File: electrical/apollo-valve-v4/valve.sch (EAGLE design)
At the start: 31 parts, among them J1 VALVE2, J2 VALVE1, U1 DRV8806-SSOP, U2 DRV8806-SSOP, U3 TPS54202

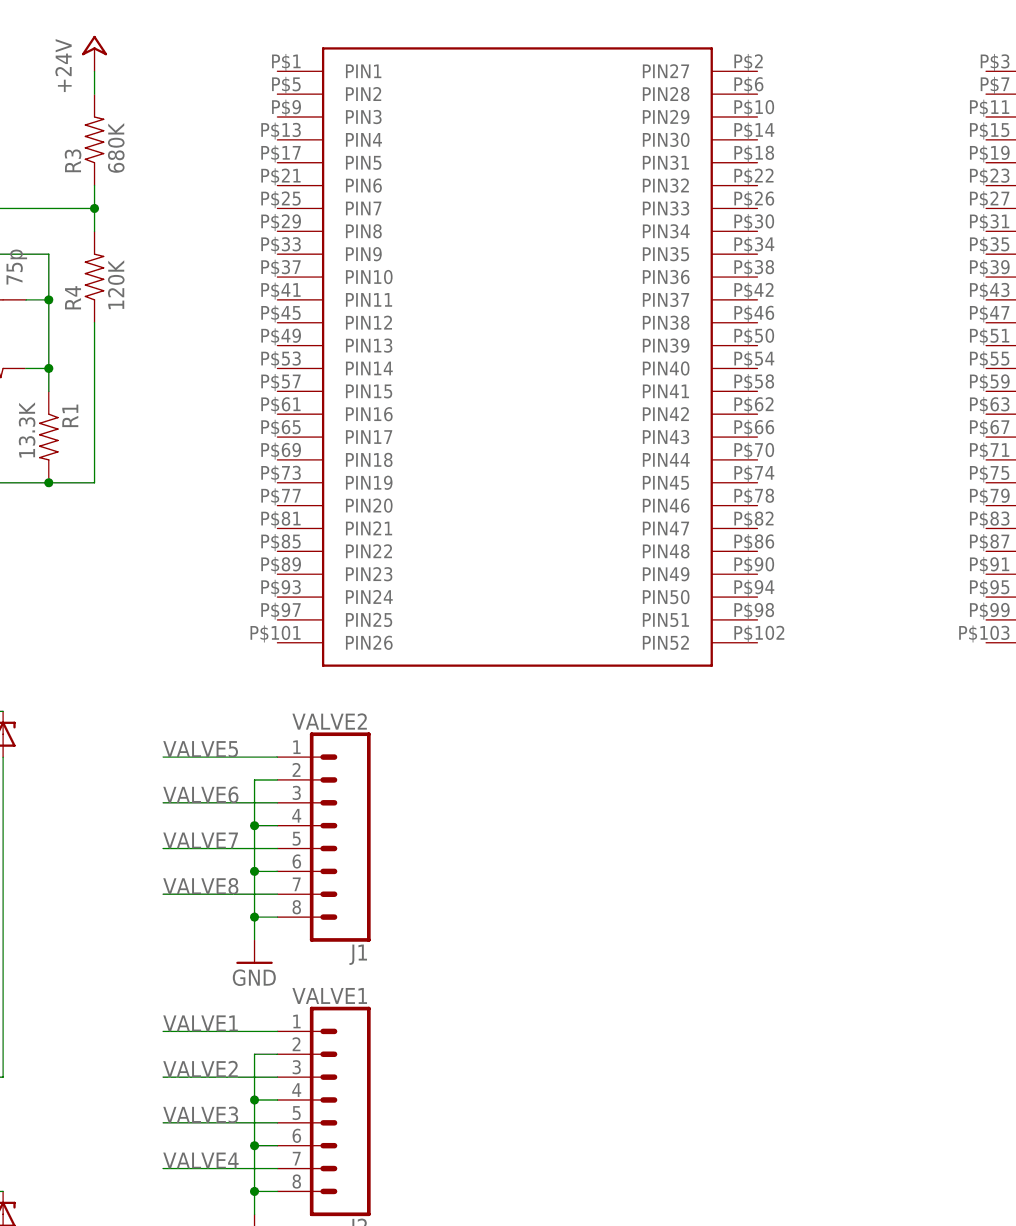
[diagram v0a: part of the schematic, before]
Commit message: Update valve board and proposed a pinout for Apollo v4
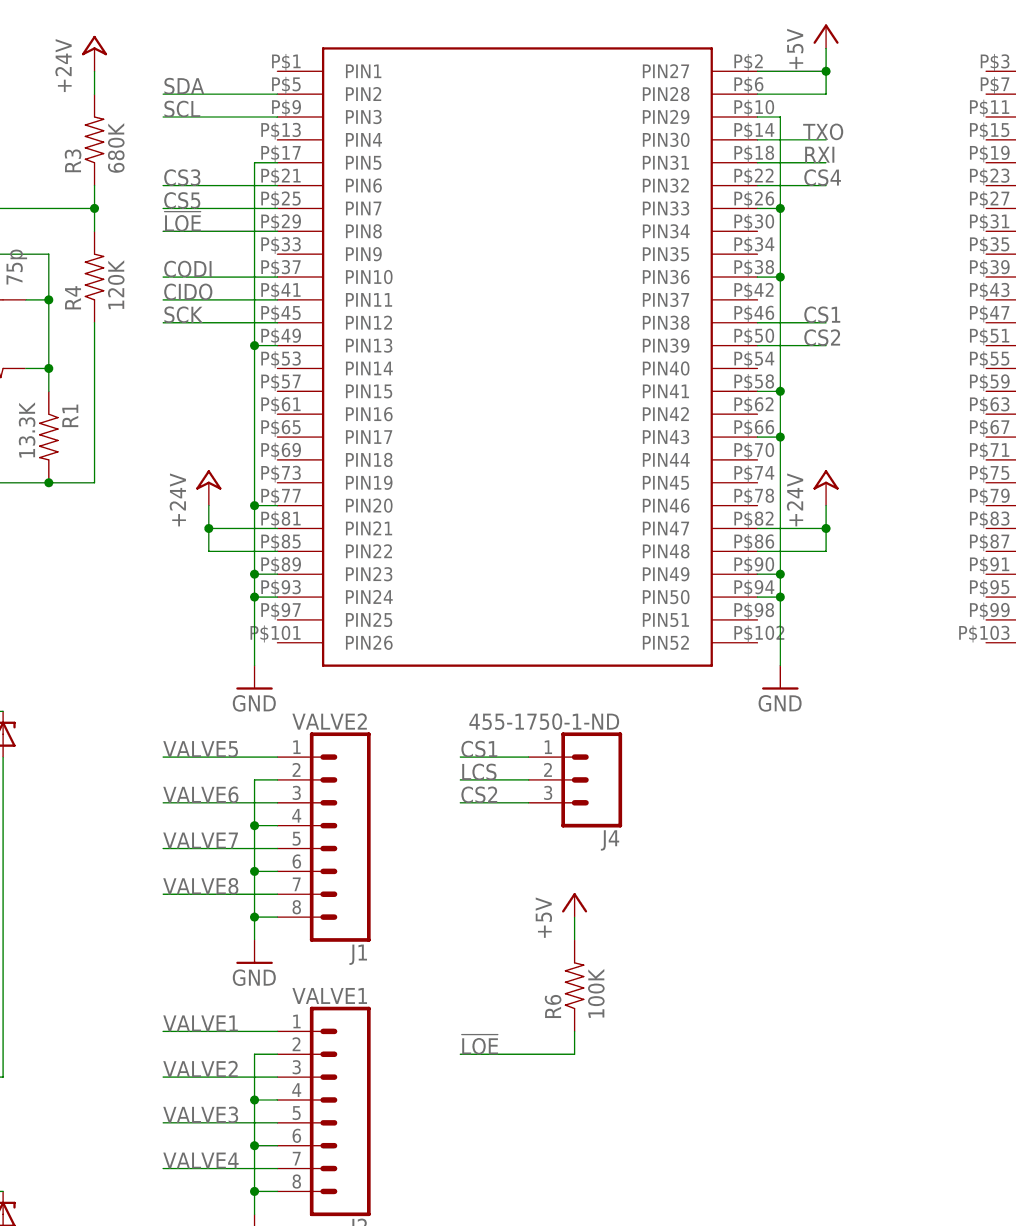
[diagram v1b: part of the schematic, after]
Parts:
- added J4: 455-1750-1-ND, SparkFun-Connectors:CONN_03
- added R6: 100K, apollo-ctrl-v4:RESISTOR0805-RES
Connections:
- new net CIDO: U$1.PIN11
- new net CS1: J4.1, U$1.PIN38
- new net CS2: J4.3, U$1.PIN39
- new net CS3: U$1.PIN6
- new net CS4: U$1.PIN32
- new net CS5: U$1.PIN7
- new net RXI: U$1.PIN31
- new net SCL: U$1.PIN3
- new net SDA: U$1.PIN2
- new net TXO: U$1.PIN30
- net !LOE!: now also R6.1, U$1.PIN8
- net +24V: now also U$1.PIN21, U$1.PIN22, U$1.PIN47, U$1.PIN48
- net +5V: now also R6.2, U$1.PIN27, U$1.PIN28
- net CODI: now also U$1.PIN10
- net GND: now also U$1.PIN13, U$1.PIN20, U$1.PIN23, U$1.PIN24, U$1.PIN29, U$1.PIN33, U$1.PIN36, U$1.PIN41, U$1.PIN43, U$1.PIN49, U$1.PIN5, U$1.PIN50
- net LCS: now also J4.2
- net SCK: now also U$1.PIN12
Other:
- note added: "DEFAULT should be CS1"

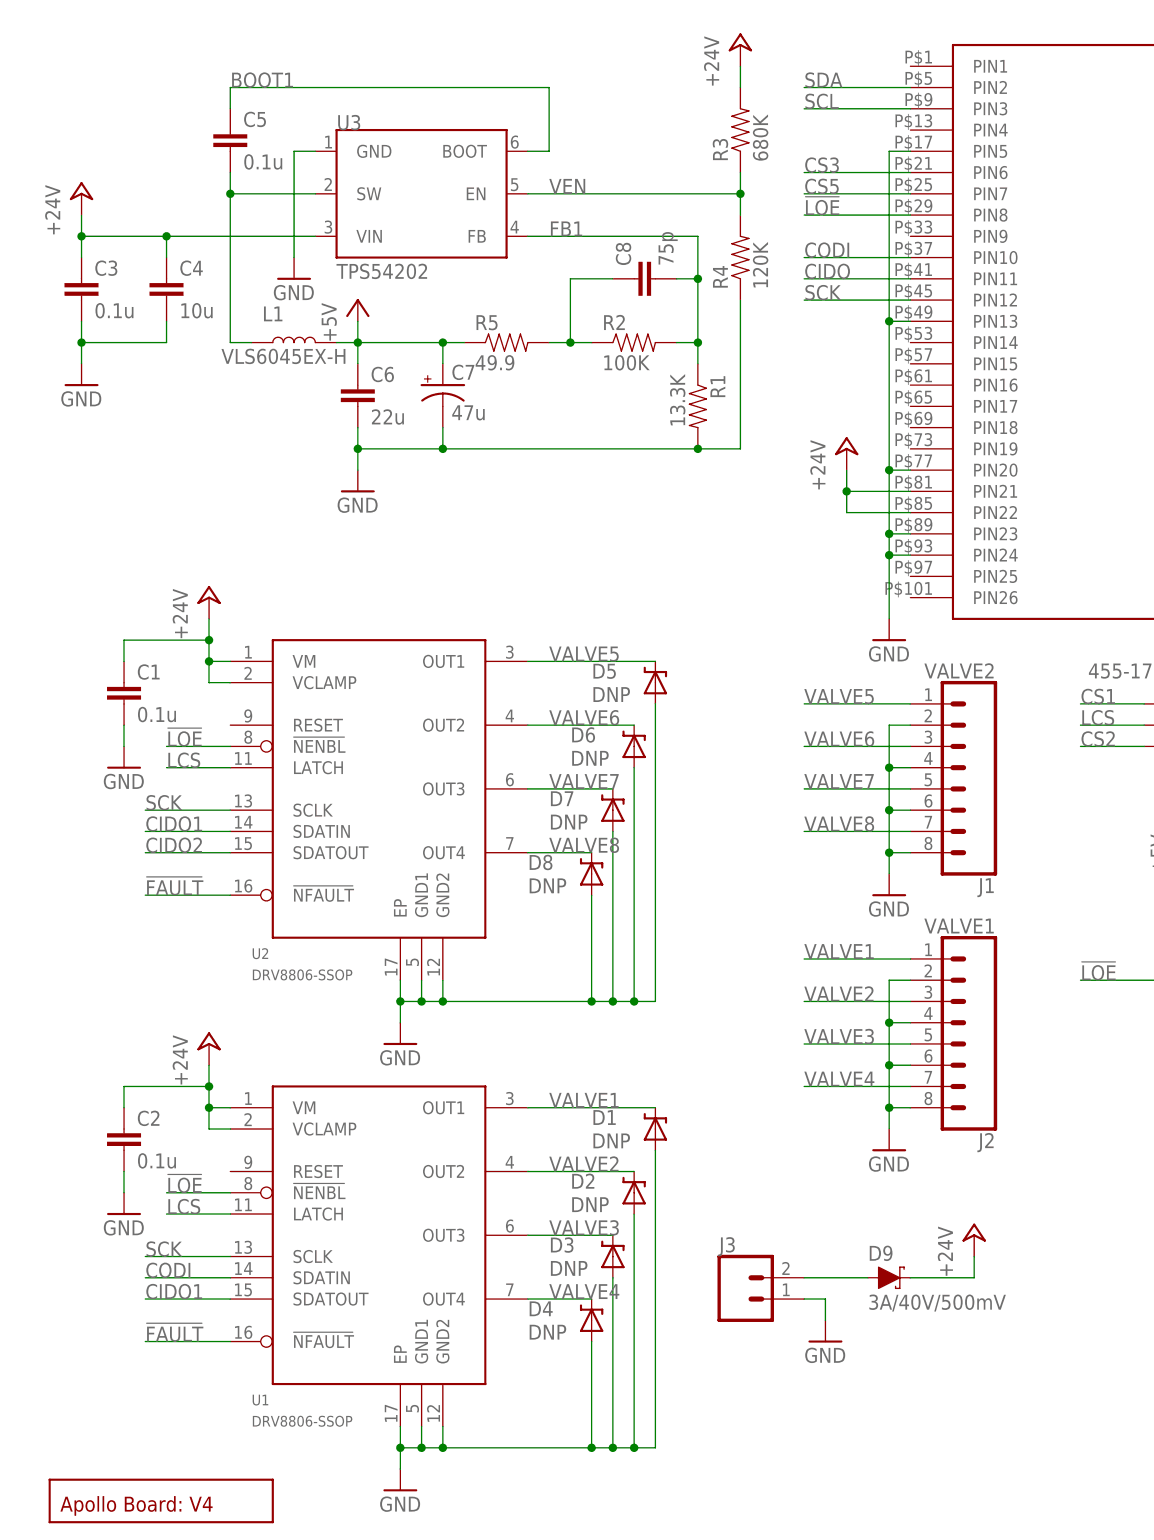
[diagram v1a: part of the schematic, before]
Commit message: Initial version of the controller board, ESP32-PICO-KIT edition. Proposed GPIO mapping also updated in the document to break out all otherwise unused pins of the ESP32.
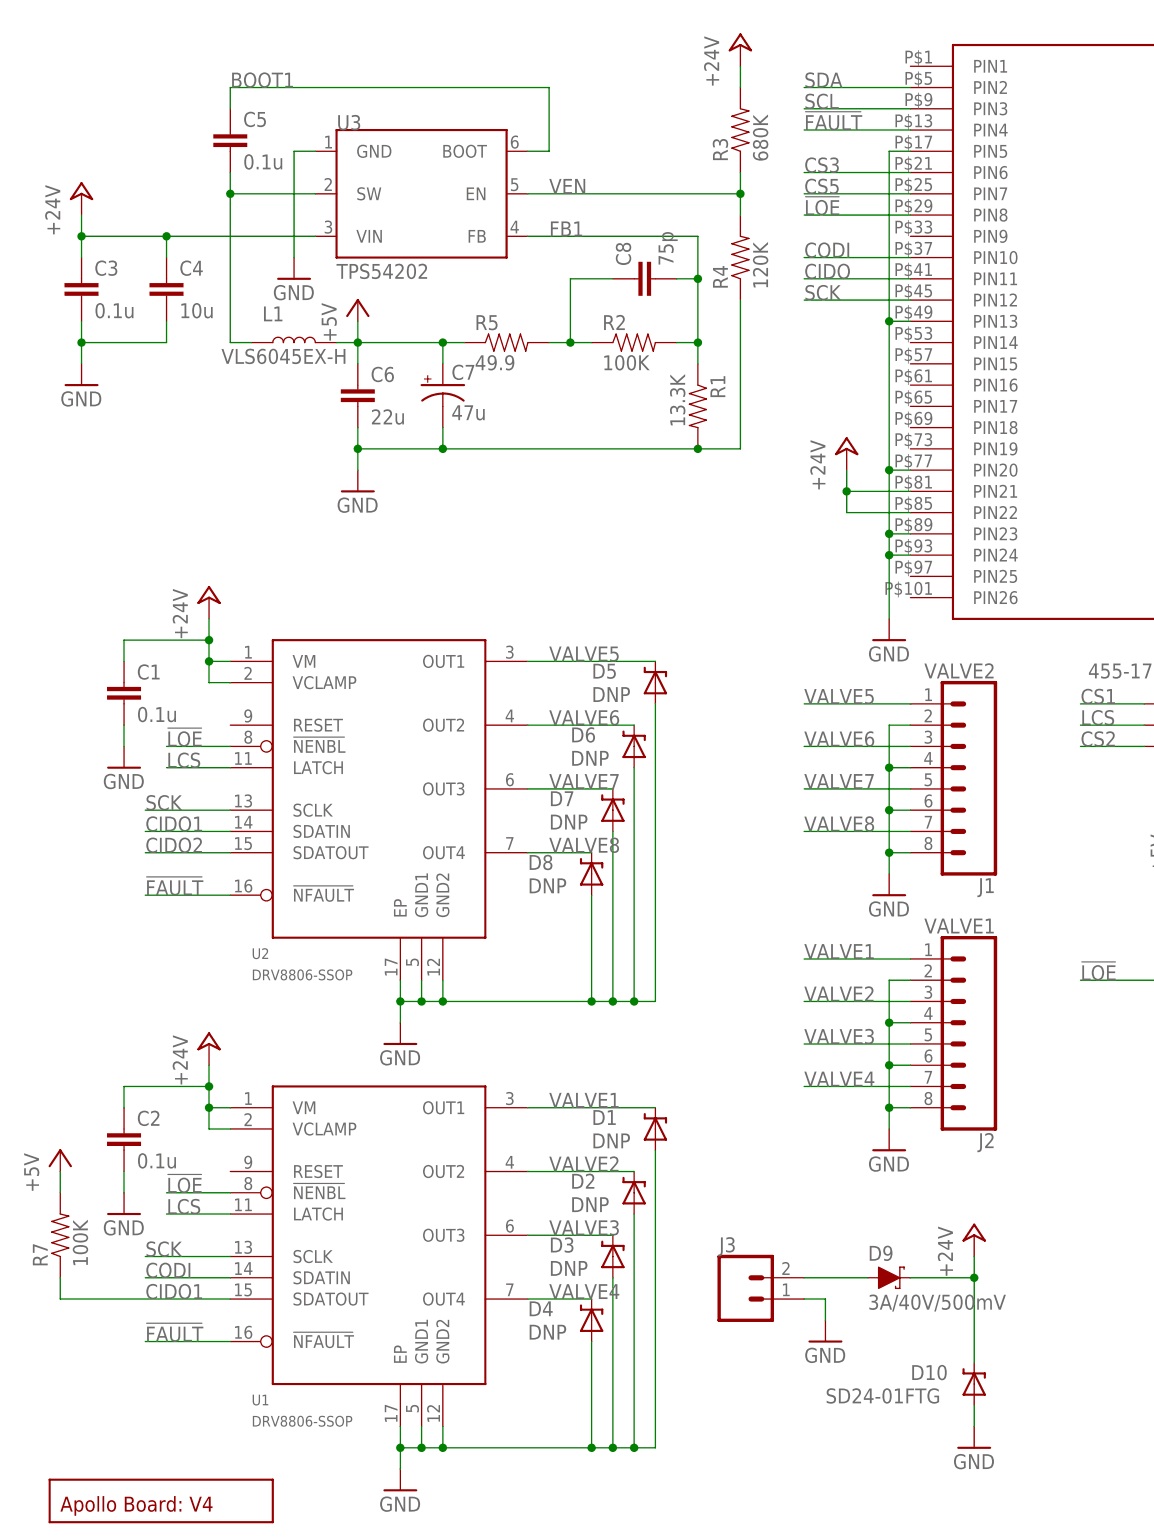
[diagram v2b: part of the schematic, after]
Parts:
- added D10: SD24-01FTG, apollo-ctrl-v4:DIODE-ZENERSOD
- added R7: 100K, apollo-ctrl-v4:RESISTOR0805-RES
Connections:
- net !FAULT!: now also U$1.PIN4
- net +24V: now also D10.C
- net +5V: now also R7.2
- net CIDO1: now also R7.1
- net GND: now also D10.A
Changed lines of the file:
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@@
 <part name="R6" library="apollo-ctrl-v4" deviceset="RESISTOR" device="0805-RES" value="100K"/>
 <part name="P+10" library="supply1" deviceset="+5V" device=""/>
+<part name="R7" library="apollo-ctrl-v4" deviceset="RESISTOR" device="0805-RES" value="100K"/>
+<part name="P+11" library="supply1" deviceset="+5V" device=""/>
+<part name="D10" library="apollo-ctrl-v4" deviceset="DIODE-ZENER" device="SOD" value="SD24-01FTG"/>
+<part name="GND13" library="supply1" deviceset="GND" device=""/>
 </parts>
 <sheets>
@@
 <instance part="R6" gate="G$1" x="139.7" y="76.2" rot="R90"/>
 <instance part="P+10" gate="1" x="139.7" y="86.36"/>
+<instance part="R7" gate="G$1" x="5.08" y="38.1" rot="R90"/>
+<instance part="P+11" gate="1" x="5.08" y="48.26"/>
+<instance part="D10" gate="G$1" x="114.3" y="20.32" smashed="yes" rot="R90">
+<attribute name="NAME" x="106.68" y="20.8026" size="1.778" layer="95"/>
+<attribute name="VALUE" x="96.52" y="18.0086" size="1.778" layer="96"/>
+</instance>
+<instance part="GND13" gate="1" x="114.3" y="12.7"/>
 </instances>
 <busses>
@@
 <junction x="104.14" y="119.38"/>
 </segment>
+<segment>
+<pinref part="GND13" gate="1" pin="GND"/>
+<pinref part="D10" gate="G$1" pin="A"/>
+<wire x1="114.3" y1="15.24" x2="114.3" y2="17.78" width="0.1524" layer="91"/>
+</segment>
 </net>
 <net name="+24V" class="0">
@@
 <wire x1="106.68" y1="33.02" x2="114.3" y2="33.02" width="0.1524" layer="91"/>
 <wire x1="114.3" y1="33.02" x2="114.3" y2="35.56" width="0.1524" layer="91"/>
+<pinref part="D10" gate="G$1" pin="C"/>
+<wire x1="114.3" y1="22.86" x2="114.3" y2="33.02" width="0.1524" layer="91"/>
+<junction x="114.3" y="33.02"/>
 </segment>
 <segment>
@@
 <label x="15.24" y="25.4" size="1.778" layer="95"/>
 </segment>
+<segment>
+<pinref part="U$1" gate="G$1" pin="PIN4"/>
+<wire x1="93.98" y1="170.18" x2="106.68" y2="170.18" width="0.1524" layer="91"/>
+<label x="93.98" y="170.18" size="1.778" layer="95"/>
+</segment>
 </net>
 <net name="SCK" class="0">
@@
 <segment>
 <pinref part="U1" gate="G$1" pin="SDATOUT"/>
-<wire x1="15.24" y1="30.48" x2="25.4" y2="30.48" width="0.1524" layer="91"/>
 <label x="15.24" y="30.48" size="1.778" layer="95"/>
+<pinref part="R7" gate="G$1" pin="1"/>
+<wire x1="25.4" y1="30.48" x2="5.08" y2="30.48" width="0.1524" layer="91"/>
+<wire x1="5.08" y1="30.48" x2="5.08" y2="33.02" width="0.1524" layer="91"/>
 </segment>
 <segment>
@@
 <wire x1="139.7" y1="81.28" x2="139.7" y2="83.82" width="0.1524" layer="91"/>
 </segment>
-</net>
+<segment>
+<pinref part="P+11" gate="1" pin="+5V"/>
+<pinref part="R7" gate="G$1" pin="2"/>
+<wire x1="5.08" y1="45.72" x2="5.08" y2="43.18" width="0.1524" layer="91"/>
+</segment>
+</net>

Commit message: Update valve board schematic
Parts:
- added C10, C15, C9: 0.1u, apollo-ctrl-v4:CAP0805
- added C11, C12, C13: 0.22u/50V, apollo-ctrl-v4:CAP0805
- added C14, C16: 0.1u/50V, apollo-ctrl-v4:CAP0805
- added C17, C18: 4700p, apollo-ctrl-v4:CAP0805
- added D11, D12, D13, D14, D15, D16, D17, D18, D19, D20, D21, D22, D23, D24, D25, D26: B340A, SparkFun-DiscreteSemi:DIODE-SCHOTTKY-B340A
- added J5: 455-1750-1-ND, SparkFun-Connectors:CONN_03
- added J6: STEPPER, SparkFun-Connectors:CONN_04SCREW
- added R10, R11, R14, R15, R16, R17, R18, R19, R20, R21: 10K, apollo-ctrl-v4:RESISTOR0805-RES
- added R12, R13: 0.1, SparkFun-Resistors:0.1OHM-1210-1/2W-1%
- added R8, R9: 100K, apollo-ctrl-v4:RESISTOR0805-RES
- added U4: TCA9534, SparkFun-IC-Conversion:TCA9534U
- added U5: DRV8811, SparkFun-IC-Special-Function:DRV8811
- added VR1: 10k, SparkFun-Resistors:TRIMPOT-PTH-10MM-KNOB-1/2W-10%
- D1, D2, D3, D4, D5, D6, D7, D8: value DNP -> B340A; device apollo-ctrl-v4:DIODE-ZENERSOD -> SparkFun-DiscreteSemi:DIODE-SCHOTTKY-B340A
- R6: value 100K -> 10K
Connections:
- new net !RESET!: R11.1, U4.P3, U5.RESETN
- new net !SM_EN!: U4.P5, U5.ENABLEN
- new net A+: D13.C, D16.A, J6.1, U5.AOUT1
- new net A-: D14.C, D15.A, J6.2, U5.AOUT2
- new net A0: J4.2, R9.2, U4.A0
- new net A1: J5.2, R8.2, U4.A1
- new net B+: D12.C, D18.A, J6.3, U5.BOUT1
- new net B-: D11.C, D17.A, J6.4, U5.BOUT2
- new net CP1: C11.1, U5.CP1
- new net CP2: C11.2, U5.CP2
- new net DECAY: C15.1, R14.2, R15.1, U5.DECAY
- new net DIR: U4.P2, U5.DIR
- new net HOME: R21.1, U4.P4, U5.HOME
- new net ISENA: R12.1, U5.ISENA
- new net ISENB: R13.1, U5.ISENB
- new net RCA: C17.1, R19.2, U5.RCA
- new net RCB: C18.1, R20.2, U5.RCB
- new net SLEEPN: R16.1, U5.SLEEPN
- new net STEP: U4.P1, U5.STEP
- new net USM0: R17.1, U4.P6, U5.USM0
- new net USM1: R18.2, U4.P7, U5.USM1
- new net VCP: C12.2, U5.VCP
- new net VGD: C13.1, U5.VGD
- new net VREF: U5.VREF, VR1.WIPER
- net !FAULT!: now also U1.!NFAULT
- net +24V: now also C12.1, C14.1, C16.1, D15.C, D16.C, D17.C, D18.C, D19.C, D20.C, D21.C, D22.C, D23.C, D24.C, D25.C, D26.C, U5.VMA, U5.VMB
- net +5V: now also C10.1, C9.1, J4.1, J5.1, R11.2, R15.2, R16.2, R18.1, U4.VCC, U5.VCC, VR1.CCW
- net CS1: no longer J4.1
- net CS2: no longer J4.3
- net CS5: now also U4.!INT
- net GND: now also C10.2, C13.2, C14.2, C15.2, C16.2, C17.2, C18.2, C9.2, D11.A, D12.A, D13.A, D14.A, J1.2, J1.4, J1.6, J1.8, J4.3, J5.3, R10.2, R12.2, R13.2, R14.1, R17.2, R19.1, R20.1, R21.2, R8.1, R9.1, U4.A2, U4.GND, U5.GND@1, U5.GND@2, U5.PAD, VR1.CW
- net LCS: now also R10.1, U4.P0; no longer J4.2
- net SCL: now also U4.SCL
- net SDA: now also U4.SDA
- net VALVE1: now also D26.A, D4.C; no longer D1.C
- net VALVE2: now also D25.A, D3.C; no longer D2.C
- net VALVE3: now also D2.C, D24.A; no longer D3.C
- net VALVE4: now also D1.C, D23.A; no longer D4.C
- net VALVE5: now also D22.A, D8.C, U2.OUT1; no longer D5.C
- net VALVE6: now also D21.A, D7.C, U2.OUT2; no longer D6.C
- net VALVE7: now also D20.A, D6.C, U2.OUT3; no longer D7.C
- net VALVE8: now also D19.A, D5.C, U2.OUT4; no longer D8.C
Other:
- note removed: "DEFAULT should be CS1"
- moved on the sheet: C1, C2, D1, D10, D2, D3, D4, D5, D6, D7, D8, D9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

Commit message: Remove stepper driver from Valve board to be moved to a future Stepper board
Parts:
- removed C10, C15, C9: 0.1u, apollo-ctrl-v4:CAP0805
- removed C11, C12, C13: 0.22u/50V, apollo-ctrl-v4:CAP0805
- removed C14, C16: 0.1u/50V, apollo-ctrl-v4:CAP0805
- removed C17, C18: 4700p, apollo-ctrl-v4:CAP0805
- removed D10: SD24-01FTG, apollo-ctrl-v4:DIODE-ZENERSOD
- removed D11, D12, D13, D14, D15, D16, D17, D18: B340A, SparkFun-DiscreteSemi:DIODE-SCHOTTKY-B340A
- removed D9: 3A/40V/500mV, SparkFun-DiscreteSemi:DIODE-SCHOTTKY-B340A
- removed J3: (no value), SparkFun-Connectors:CONN_023.5MM
- removed J4, J5: 455-1750-1-ND, SparkFun-Connectors:CONN_03
- removed J6: STEPPER, SparkFun-Connectors:CONN_04SCREW
- removed R10, R11, R14, R15, R16, R17, R18, R19, R20, R21: 10K, apollo-ctrl-v4:RESISTOR0805-RES
- removed R12, R13: 0.1, SparkFun-Resistors:0.1OHM-1210-1/2W-1%
- removed R8, R9: 100K, apollo-ctrl-v4:RESISTOR0805-RES
- removed U4: TCA9534, SparkFun-IC-Conversion:TCA9534U
- removed U5: DRV8811, SparkFun-IC-Special-Function:DRV8811
- removed VR1: 10k, SparkFun-Resistors:TRIMPOT-PTH-10MM-KNOB-1/2W-10%
- added J7: 455-1750-1-ND, SparkFun-Connectors:CONN_03
- R6: value 10K -> 100K
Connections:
- removed net !RESET!: R11.1, U4.P3, U5.RESETN
- removed net !SM_EN!: U4.P5, U5.ENABLEN
- removed net A+: D13.C, D16.A, J6.1, U5.AOUT1
- removed net A-: D14.C, D15.A, J6.2, U5.AOUT2
- removed net A0: J4.2, R9.2, U4.A0
- removed net A1: J5.2, R8.2, U4.A1
- removed net B+: D12.C, D18.A, J6.3, U5.BOUT1
- removed net B-: D11.C, D17.A, J6.4, U5.BOUT2
- removed net CIDO2: U2.SDATOUT
- removed net CP1: C11.1, U5.CP1
- removed net CP2: C11.2, U5.CP2
- removed net DECAY: C15.1, R14.2, R15.1, U5.DECAY
- removed net DIR: U4.P2, U5.DIR
- removed net HOME: R21.1, U4.P4, U5.HOME
- removed net ISENA: R12.1, U5.ISENA
- removed net ISENB: R13.1, U5.ISENB
- removed net RCA: C17.1, R19.2, U5.RCA
- removed net RCB: C18.1, R20.2, U5.RCB
- removed net SLEEPN: R16.1, U5.SLEEPN
- removed net STEP: U4.P1, U5.STEP
- removed net USM0: R17.1, U4.P6, U5.USM0
- removed net USM1: R18.2, U4.P7, U5.USM1
- removed net VCP: C12.2, U5.VCP
- removed net VGD: C13.1, U5.VGD
- removed net VIN: D9.A, J3.2
- removed net VREF: U5.VREF, VR1.WIPER
- net !LOE!: no longer R6.1
- net +24V: no longer C12.1, C14.1, C16.1, D10.C, D15.C, D16.C, D17.C, D18.C, D9.C, U5.VMA, U5.VMB
- net +5V: no longer C10.1, C9.1, J4.1, J5.1, R11.2, R15.2, R16.2, R18.1, R6.2, U4.VCC, U5.VCC, VR1.CCW
- net CIDO: now also U2.SDATOUT
- net CS1: now also J7.1, R6.2
- net CS2: now also J7.3
- net CS5: no longer U4.!INT
- net GND: no longer C10.2, C13.2, C14.2, C15.2, C16.2, C17.2, C18.2, C9.2, D10.A, D11.A, D12.A, D13.A, D14.A, J3.1, J4.3, J5.3, R10.2, R12.2, R13.2, R14.1, R17.2, R19.1, R20.1, R21.2, R8.1, R9.1, U4.A2, U4.GND, U5.GND@1, U5.GND@2, U5.PAD, VR1.CW
- net LCS: now also J7.2, R6.1; no longer R10.1, U4.P0
- net SCL: no longer U4.SCL
- net SDA: no longer U4.SDA
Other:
- moved on the sheet: R6
